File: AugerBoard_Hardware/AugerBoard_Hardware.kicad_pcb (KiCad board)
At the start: 2 copper layers, 44 parts, among them J1 RJ45_LED_Shielded, J2 Conn_01x04_MountingPin, Q1 BSS138, Q2 BSS138, Q3 BSS138, SW1 SW_SPDT, SW2 SW_Push, SW3 SW_Push, SW4 SW_Push, U1 Teensy4.1_DEV-16771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

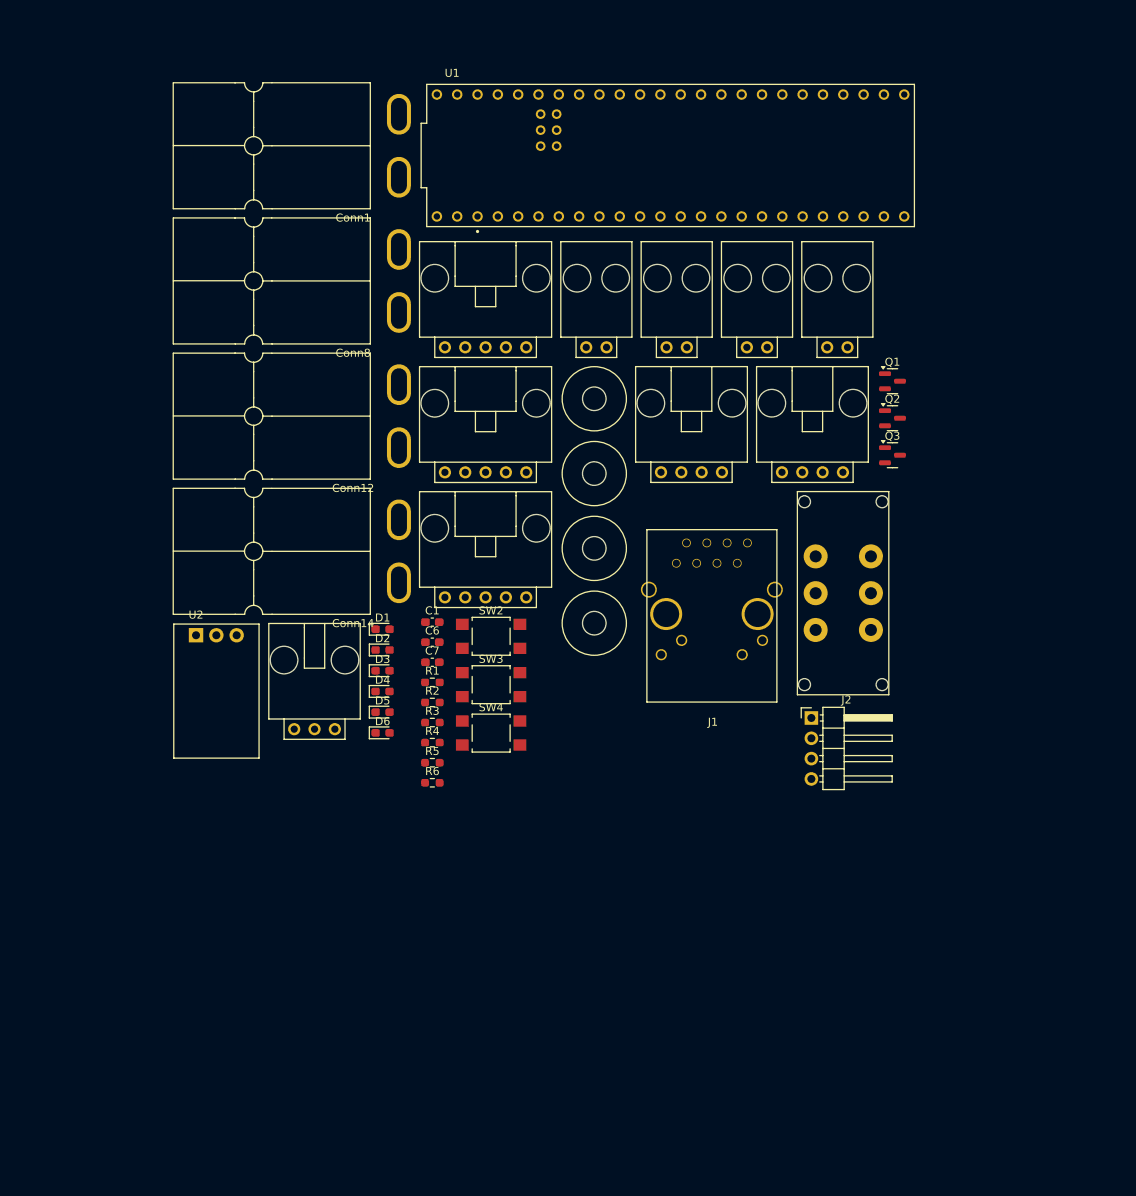
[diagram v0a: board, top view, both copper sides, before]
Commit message: Footprint changed and layout started
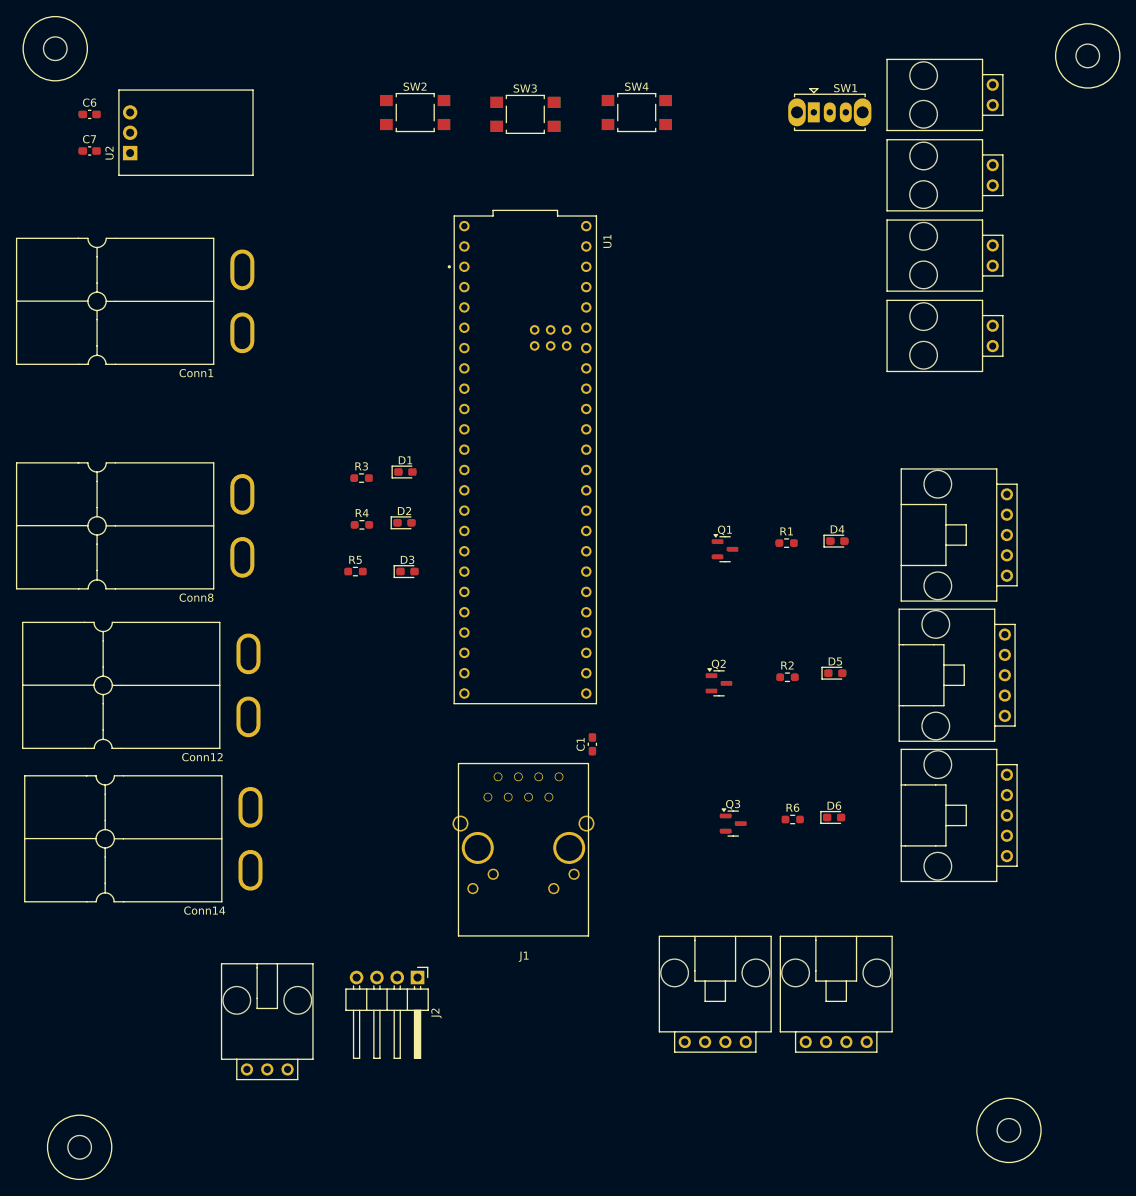
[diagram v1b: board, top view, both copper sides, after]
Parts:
- SW1: footprint MRDT_Switches:1P2T_Angled_Slide_GPI-152-3013 -> Button_Switch_THT:SW_Slide_SPDT_Straight_CK_OS102011MS2Q
- moved H2 94.8 mm to (85.0, 171.1), turned to 180 degrees
- moved H3 87.1 mm to (202.9, 42.7)
- moved SW4 79.7 mm to (150.6, 45.7)
- moved C6 78.7 mm to (82.2, 46.0)
- moved Conn15 77.3 mm to (196.8, 138.7), turned to 90 degrees
- moved C7 76.9 mm to (82.2, 50.5)
- moved Conn13 76.3 mm to (196.6, 121.2), turned to 90 degrees
- moved H4 75.9 mm to (193.1, 169.0), turned to -90 degrees
- moved Conn9 75.8 mm to (196.8, 103.6), turned to 90 degrees
- moved H1 73.7 mm to (81.9, 41.8), turned to 90 degrees
- moved SW3 71.4 mm to (136.7, 46.0)
- moved Conn2 71.3 mm to (156.6, 161.9)
- moved Conn3 71.3 mm to (171.7, 161.9)
- moved SW2 66.2 mm to (122.9, 45.7)
- moved U2 60.8 mm to (87.3, 50.8), turned to 90 degrees
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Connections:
- C1 pad 1: LimitSwitch1 -> GND
- C6 pad 2: LimitSwitch1 -> GND
- C7 pad 2: LimitSwitch1 -> GND
- Conn1 pad 1: LimitSwitch1 -> GND
- Conn10 pad 2: LimitSwitch1 -> LimitSwitch3
- Conn11 pad 2: LimitSwitch1 -> LimitSwitch4
- Conn12 pad 1: LimitSwitch1 -> GND
- Conn14 pad 1: LimitSwitch1 -> GND
- Conn2 pad 4: LimitSwitch1 -> GND
- Conn3 pad 4: LimitSwitch1 -> GND
- Conn5 pad 2: LimitSwitch1 -> LimitSwitch2
- Conn7 pad 3: LimitSwitch1 -> GND
- Conn8 pad 1: LimitSwitch1 -> GND
- D1 pad 1: LimitSwitch1 -> GND
- D2 pad 1: LimitSwitch1 -> GND
- D3 pad 1: LimitSwitch1 -> GND
- J1 pad 8: LimitSwitch1 -> GND
- J1 pad 9: LimitSwitch1 -> GND
- J1 pad SH: LimitSwitch1 -> GND
- J2 pad 2: LimitSwitch1 -> GND
- J2 pad 4: LimitSwitch1 -> GND
- Q1 pad 2: LimitSwitch1 -> GND
- Q2 pad 2: LimitSwitch1 -> GND
- Q3 pad 2: LimitSwitch1 -> GND
- SW1 pad 3: LimitSwitch1 -> GND
- SW2 pad 2: LimitSwitch1 -> GND
- SW3 pad 2: LimitSwitch1 -> GND
- SW4 pad 2: LimitSwitch1 -> GND
- U1 pad 1: LimitSwitch1 -> LimitSwitch2
- U1 pad 7: LimitSwitch1 -> LimitSwitch3
- U1 pad 8: LimitSwitch1 -> LimitSwitch4
- U1 pad GND1: LimitSwitch1 -> GND
- U1 pad GND2: LimitSwitch1 -> GND
- U1 pad GND3: LimitSwitch1 -> GND
- U1 pad GND5: LimitSwitch1 -> GND
- U2 pad 2: LimitSwitch1 -> GND

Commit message: Layout fun time yippie #based #awesome
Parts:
- J2: footprint Connector_PinHeader_2.54mm:PinHeader_1x04_P2.54mm_Horizontal -> Connector_PinHeader_2.54mm:PinHeader_1x04_P2.54mm_Vertical
- R1, R2, R6: value 200 -> 220
- moved C6 70.8 mm to (114.3, 109.1), turned to 90 degrees
- moved J2 69.3 mm to (171.4, 104.1), turned to 0 degrees
- moved C7 69.1 mm to (118.9, 109.1), turned to 90 degrees
- moved Conn11 65.9 mm to (188.1, 110.4), turned to -90 degrees
- moved D6 59.3 mm to (155.6, 77.9)
- moved Q3 56.5 mm to (150.2, 79.5)
- moved R6 55.6 mm to (155.6, 80.5)
- moved U2 49.0 mm to (120.9, 86.5), turned to 180 degrees
- moved D5 49.0 mm to (144.7, 77.7)
- moved D4 47.2 mm to (133.7, 77.7)
- moved Conn10 44.8 mm to (188.1, 99.1), turned to -90 degrees
- moved R2 43.8 mm to (144.7, 80.2)
- moved Q2 43.6 mm to (139.3, 79.2)
- moved U1 41.8 mm to (147.3, 129.5), turned to 0 degrees
- moved R1 40.5 mm to (133.7, 80.3)
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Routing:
- added copper zone on B.Cu, net +12V
- added copper zone on F.Cu, net +12V

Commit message: Layout made smaller hai
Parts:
- Conn10, Conn11, Conn4, Conn5: footprint MRDT_Connectors:MOLEX_SL_02_Horizontal -> MRDT_Connectors:MOLEX_SL_02_Vertical
- Conn13, Conn15, Conn9: footprint MRDT_Connectors:MOLEX_SL_05_Horizontal -> MRDT_Connectors:MOLEX_SL_05_Vertical
- Conn2, Conn3: footprint MRDT_Connectors:MOLEX_SL_04_Horizontal -> MRDT_Connectors:MOLEX_SL_04_Vertical
- Conn7: footprint MRDT_Connectors:MOLEX_SL_03_Horizontal -> MRDT_Connectors:MOLEX_SL_03_Vertical
- moved Conn3 94.3 mm to (128.3, 74.9), turned to -90 degrees
- moved Conn4 88.8 mm to (133.4, 146.3), turned to 0 degrees
- moved Conn2 83.4 mm to (122.2, 82.5), turned to 90 degrees
- moved Conn5 79.0 mm to (145.6, 154.3), turned to 180 degrees
- moved Conn11 68.4 mm to (135.7, 154.3), turned to 180 degrees
- moved Conn10 65.2 mm to (143.2, 146.3), turned to 0 degrees
- moved H3 50.2 mm to (169.6, 80.1)
- moved SW1 39.8 mm to (135.6, 74.9), turned to -90 degrees
- moved D1 38.5 mm to (100.1, 96.9), turned to -90 degrees
- moved D2 37.1 mm to (102.4, 96.9), turned to -90 degrees
- moved D3 36.8 mm to (104.6, 97.0), turned to -90 degrees
- moved Conn13 35.4 mm to (153.2, 146.6), turned to 0 degrees
- moved R3 33.0 mm to (100.1, 100.8), turned to 90 degrees
- moved R4 31.3 mm to (102.4, 100.8), turned to 90 degrees
- moved R5 29.5 mm to (104.6, 100.8), turned to 90 degrees
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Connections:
- Conn1 pad 4: (no net) -> +12V
- Conn12 pad 4: (no net) -> +12V
- Conn8 pad 4: (no net) -> +12V
- U1 pad 3.3V_1: unconnected-(U1-3.3V-Pad3.3V_1)_1 -> +3.3V
- U1 pad 3.3V_2: unconnected-(U1-3.3V-Pad3.3V_1) -> +3.3V
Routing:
- net Net-(D2-A): track 0.00 -> 2.17 mm
- net Net-(D1-A): track 0.00 -> 2.11 mm
- net Net-(D3-A): track 0.00 -> 2.08 mm
- added copper zone on B.Cu, net GND
- added copper zone on F.Cu, net GND

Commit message: Good first pass hai
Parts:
- moved J2 43.3 mm to (173.2, 135.4)
- moved D6 16.9 mm to (163.0, 95.6), turned to 180 degrees
- moved R6 16.9 mm to (163.0, 98.2), turned to 180 degrees
- moved SW4 16.9 mm to (160.1, 91.4)
- moved Q3 16.9 mm to (157.6, 97.2)
- moved D1 8.02 mm to (103.6, 104.1), turned to 180 degrees
- moved R5 6.70 mm to (99.8, 96.3), turned to 0 degrees
- moved Q2 6.12 mm to (157.5, 79.9)
- moved SW3 6.10 mm to (160.0, 74.7)
- moved R2 6.10 mm to (162.9, 81.5), turned to 180 degrees
- moved D5 5.99 mm to (162.8, 79.0), turned to 180 degrees
- moved D2 3.67 mm to (103.6, 100.3), turned to 180 degrees
- moved R3 3.31 mm to (99.7, 104.1), turned to 0 degrees
- moved SW2 3.15 mm to (146.8, 74.7)
- moved Q1 3.15 mm to (144.0, 80.0)
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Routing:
- net +3.3V: track 0.00 -> 196.8 mm, vias 0 -> 7
- net PWM1: track 0.00 -> 107.9 mm, vias 0 -> 3
- net PWM3: track 0.00 -> 85.5 mm, vias 0 -> 4
- net Temp: track 0.00 -> 85.4 mm, vias 0 -> 1
- net PWM2: track 0.00 -> 79.0 mm, vias 0 -> 3
- net GND: track 0.00 -> 72.5 mm, vias 0 -> 1
- net IN_B3: track 0.00 -> 63.7 mm, vias 0 -> 2
- net LimitSwitch2: track 0.00 -> 60.8 mm, vias 0 -> 2
- net LED: track 0.00 -> 58.9 mm, vias 0 -> 1
- net Humidity: track 0.00 -> 51.1 mm
- net LimitSwitch1: track 0.00 -> 51.0 mm, vias 0 -> 2
- net IN_A3: track 0.00 -> 50.8 mm
- net IN_A1: track 0.00 -> 50.6 mm, vias 0 -> 1
- net Dir_Switch: track 0.00 -> 47.2 mm, vias 0 -> 2
- net T+: track 0.00 -> 43.6 mm, vias 0 -> 1
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- removed copper zone on B.Cu, net +12V
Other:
- board outline added: 103.1 x 87.6 mm

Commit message: Layout made smaller h
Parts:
- moved Conn2 67.1 mm to (159.1, 138.6), turned to 180 degrees
- moved Conn3 59.9 mm to (151.5, 130.2), turned to 0 degrees
- moved J2 48.1 mm to (160.4, 89.0)
- moved D5 28.5 mm to (134.4, 79.0)
- moved SW3 28.4 mm to (131.6, 74.7)
- moved R2 28.3 mm to (134.6, 81.5)
- moved Q2 28.3 mm to (129.2, 79.9)
- moved Q1 25.6 mm to (118.4, 80.0)
- moved SW2 25.6 mm to (121.2, 74.6)
- moved R1 25.5 mm to (124.2, 81.5)
- moved D4 25.5 mm to (124.2, 79.0)
- moved R6 24.6 mm to (145.1, 81.3)
- moved SW4 24.6 mm to (142.2, 74.6)
- moved Q3 24.5 mm to (139.7, 80.5)
- moved D6 24.4 mm to (145.1, 79.0)
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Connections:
- Conn1 pad 4: +12V -> (no net)
- Conn12 pad 4: +12V -> (no net)
- Conn14 pad : +12V -> (no net)
- Conn8 pad 4: +12V -> (no net)
- U1 pad 41: SEL3 -> unconnected-(U1-A17-Pad41)
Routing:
- net +5V: track 29.7 -> 116.4 mm, vias 0 -> 1
- net SW1: track 7.20 -> 80.9 mm, vias 0 -> 4
- net GND: track 72.5 -> 0.00 mm, vias 1 -> 0
- net LED: track 58.9 -> 0.00 mm, vias 1 -> 0
- net SW2: track 7.20 -> 63.4 mm, vias 0 -> 4
- net SW3: track 7.20 -> 51.4 mm
- net Encoder_2b: track 28.9 -> 61.2 mm, vias 0 -> 2
- net Temp: track 85.4 -> 58.6 mm
- net LimitSwitch3: track 42.9 -> 16.6 mm, vias 2 -> 1
- net LimitSwitch1: track 51.0 -> 25.6 mm, vias 2 -> 1
- net PWM1: track 107.9 -> 85.5 mm, vias 3 -> 2
- net IN_B3: track 63.7 -> 42.3 mm, vias 2 -> 0
- net LimitSwitch2: track 60.8 -> 40.1 mm
- net Encoder_2a: track 31.0 -> 51.3 mm, vias 0 -> 1
- net Encoder_1a: track 40.4 -> 58.8 mm, vias 2 -> 1
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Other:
- board size 103.1 x 87.6 mm -> 87.2 x 81.9 mm

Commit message: i dont know what is happening
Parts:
- added  : LOGO, LOGO, F.Cu at (142.5, 91.2)
- added ‎: LOGO, LOGO, F.Cu at (81.0, 86.4)
- added ‎ : LOGO, LOGO, F.Cu at (86.9, 148.8)
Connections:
- Conn1 pad 4: (no net) -> +12V
- Conn12 pad 4: (no net) -> +12V
- Conn14 pad : (no net) -> +12V
- Conn8 pad 4: (no net) -> +12V
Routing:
- net +3.3V: track 212.5 -> 213.7 mm
- net +5V: track 116.4 -> 117.0 mm

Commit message: Layout finished?
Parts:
- added G***: LOGO, LOGO, F.Cu at (136.1, 98.0)
- added G***: LOGO, LOGO, B.Cu at (128.0, 137.2)
-  : moved to B.Cu
- moved ‎ 65.8 mm to (145.8, 98.0)
- moved   51.3 mm to (148.0, 142.3), turned to 180 degrees
- moved SW1 2.86 mm to (150.4, 77.5)
- moved C1 1.52 mm to (111.8, 128.6)
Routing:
- net LED: track 0.00 -> 48.0 mm, vias 0 -> 1
- net +12V: track 6.66 -> 45.1 mm, vias 0 -> 2
- net +3.3V: track 213.7 -> 246.8 mm
- net T+: track 46.1 -> 39.2 mm, vias 1 -> 0
- net T-: track 46.0 -> 39.1 mm, vias 1 -> 0
- net Dir_Switch: track 57.5 -> 54.6 mm
- net Net-(C1-Pad2): track 16.8 -> 18.4 mm
- net R+: track 29.1 -> 27.7 mm
- net R-: track 29.2 -> 27.7 mm
- net SW3: track 51.4 -> 52.2 mm
- net GND: vias 0 -> 58
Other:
- board text added: "Auger Board Rev1 Mars Rover Design Team Missouri S&T, 2025 Angel Espinoza-Mendoza Timothy Lipina"

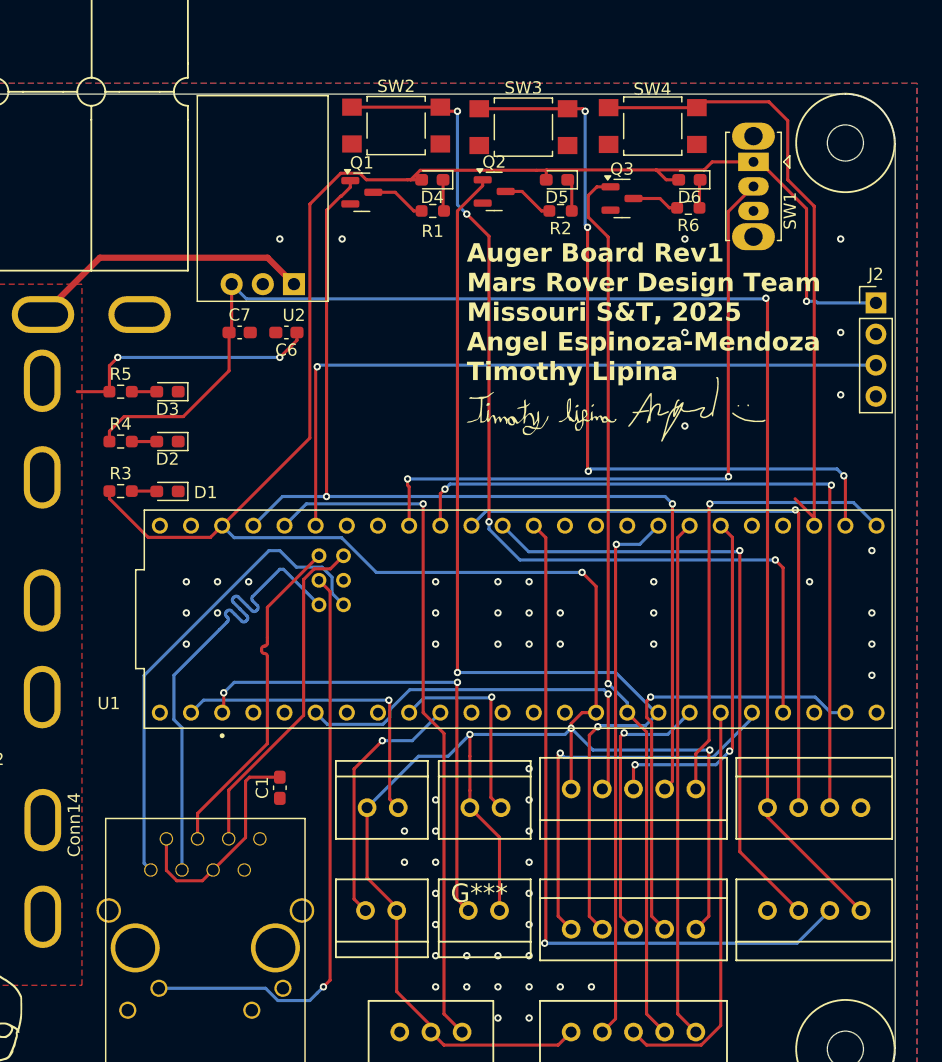
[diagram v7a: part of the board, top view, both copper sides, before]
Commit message: Fixed various clearances and silkscreen issues. Many still persist
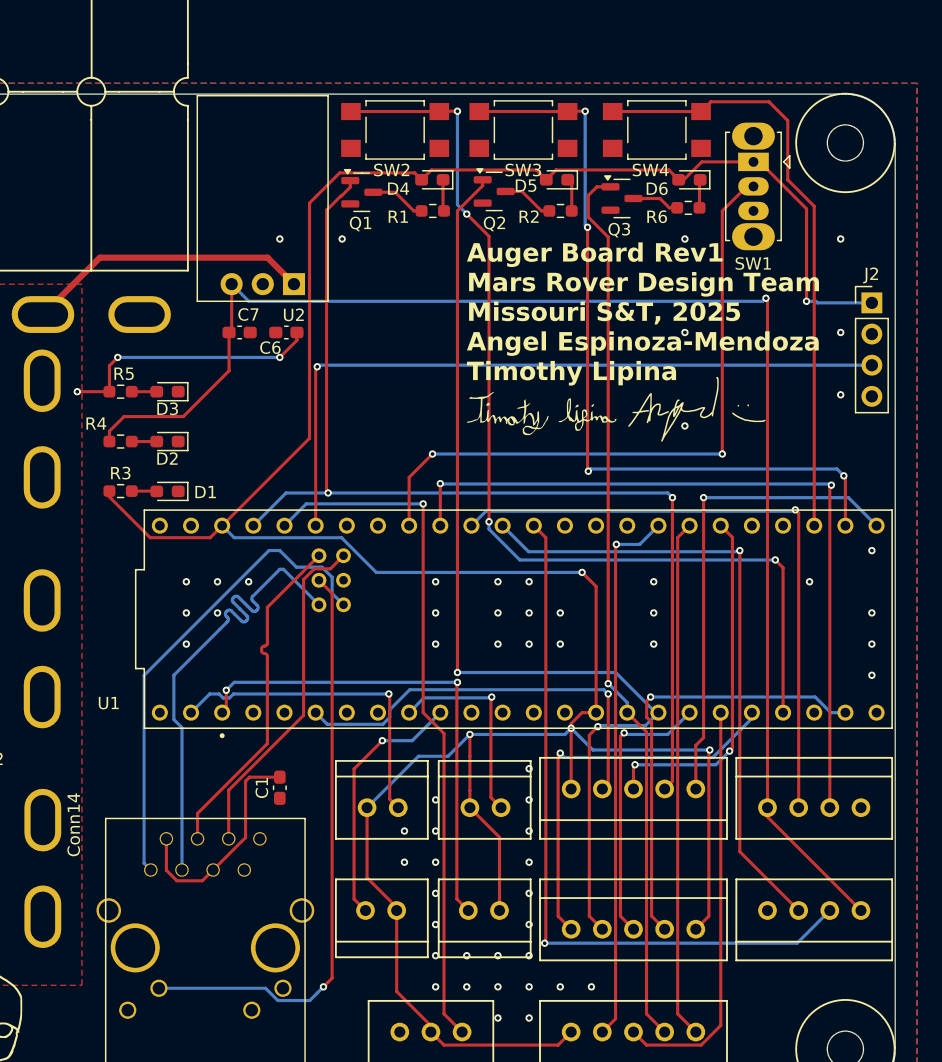
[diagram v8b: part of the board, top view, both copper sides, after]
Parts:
- moved SW4 0.46 mm to (142.5, 74.9)
- moved SW2 0.37 mm to (121.2, 74.9)
- moved J2 0.33 mm to (160.0, 89.0)
- moved SW3 0.23 mm to (131.6, 74.9)
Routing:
- net +3.3V: track 246.8 -> 244.0 mm
- net SW3: track 52.2 -> 49.8 mm
- net Dir_Switch: track 54.6 -> 53.4 mm
- net LimitSwitch1: track 25.6 -> 26.6 mm
- net IN_B1: track 38.1 -> 39.1 mm
- net Encoder_2b: track 61.2 -> 61.7 mm
- net +12V: vias 2 -> 3
